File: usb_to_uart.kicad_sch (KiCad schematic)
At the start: 23 parts

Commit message: v1
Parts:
- gave numbers to parts that had none: 23

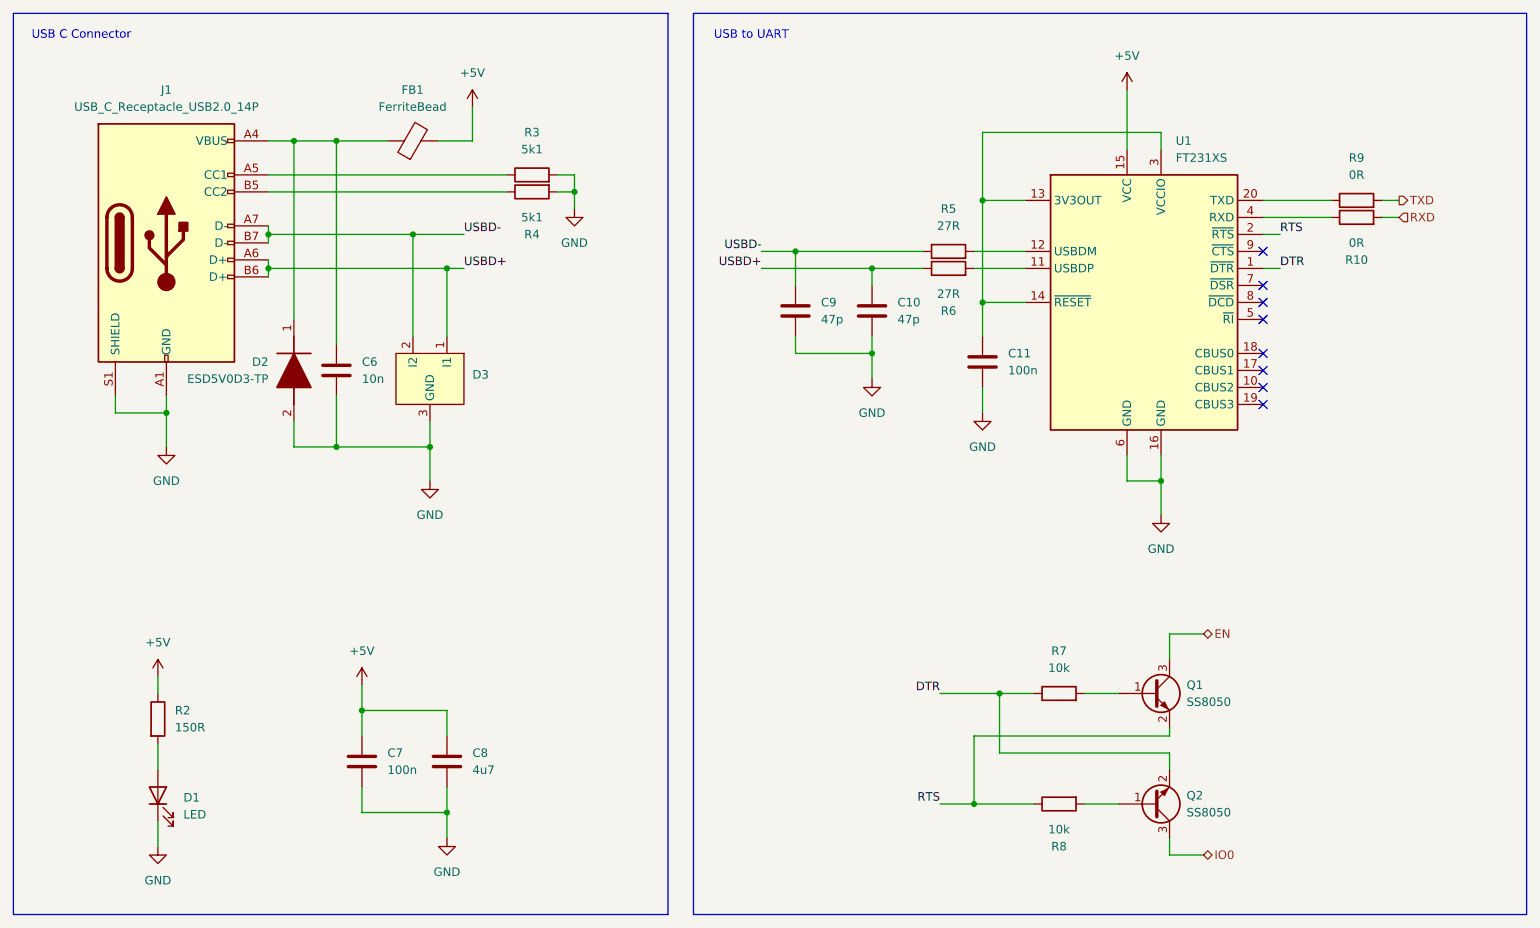
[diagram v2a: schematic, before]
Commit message: passed drc (somehow)
board routing is def cooked
verify:
- boost layout
- usb terminal layout
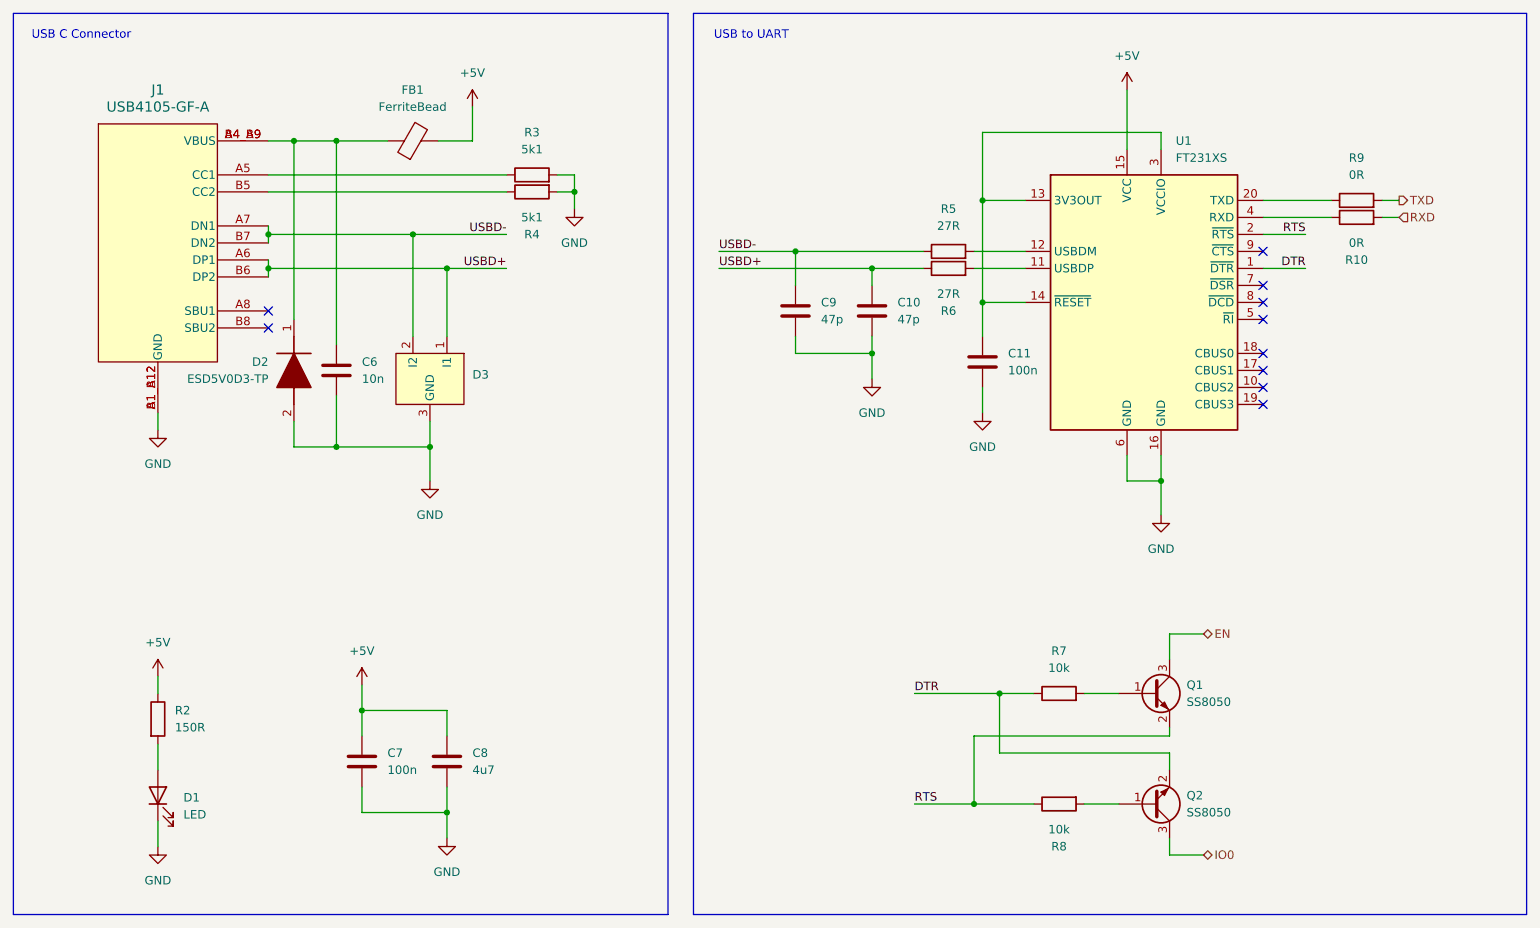
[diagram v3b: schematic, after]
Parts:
- removed J1: USB_C_Receptacle_USB2.0_14P, symbol Connector:USB_C_Receptacle_USB2.0_14P
- added J1: USB4105-GF-A, footprints:GCT_USB4105-GF-A, symbol usbc:USB4105-GF-A
- C10, C11, C6, C7, C8, C9: footprint (none) -> Capacitor_SMD:C_0603_1608Metric_Pad1.08x0.95mm_HandSolder
- D1: footprint LED_SMD:LED_1206_3216Metric -> LED_SMD:LED_1206_3216Metric_Pad1.42x1.75mm_HandSolder
- D2: footprint SOD2512X115N -> footprints:ESD5V0D3-TP
- D3: footprint (none) -> Package_TO_SOT_SMD:SOT-23-3
- R10, R2, R3, R4, R5, R6, R7, R8, R9: footprint (none) -> Resistor_SMD:R_0603_1608Metric
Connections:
- net GND: now also J1.A1_B12 (GND), J1.B1_A12 (GND)
- net USBD+: now also J1.A6 (DP1), J1.B6 (DP2)
- net USBD-: now also J1.A7 (DN1), J1.B7 (DN2)
- net at C6.1, D2.1 (K), FB1.1: now also J1.A4_B9 (VBUS), J1.B4_A9 (VBUS)
- net at R3.1: now also J1.A5 (CC1)
- net at R4.1: now also J1.B5 (CC2)
- no-connect marks 8 -> 10
